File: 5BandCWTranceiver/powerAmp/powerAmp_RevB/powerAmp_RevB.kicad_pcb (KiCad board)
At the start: 2 copper layers, 59.7 x 45.7 mm, 56 parts, among them Q1 IRF530, Q5 2N2907SOT223, Q6 MOSFET-NCHANNELBS170, T1 2N2222A-SOT223, T2 2N2222A-SOT223

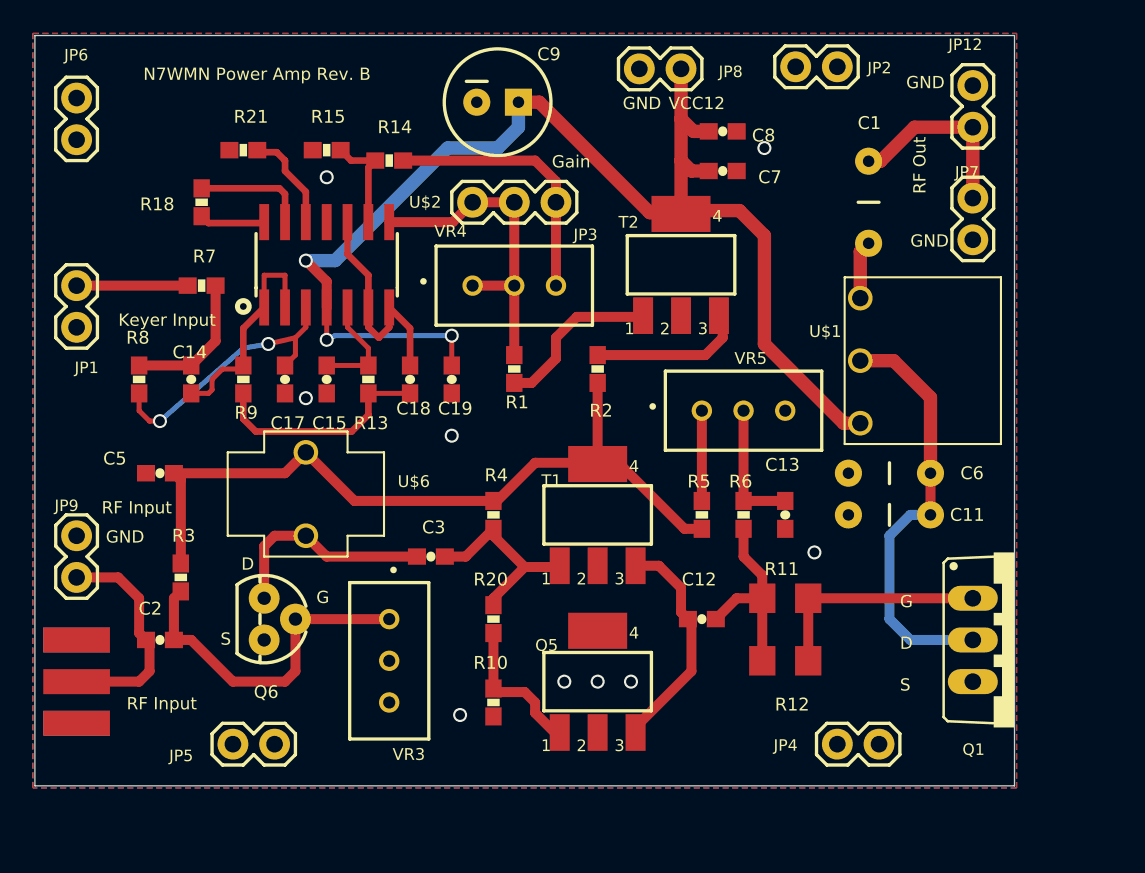
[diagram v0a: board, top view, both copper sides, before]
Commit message: Removed zip files
remove zip files
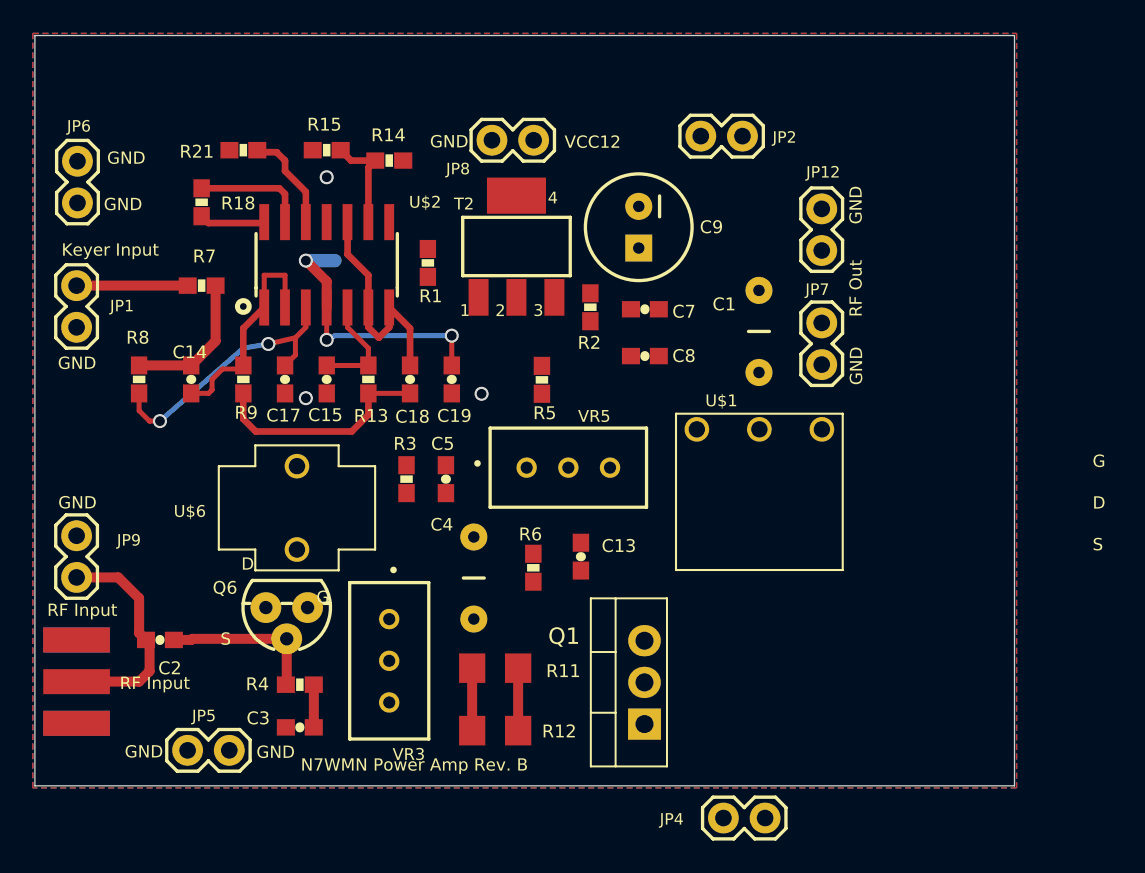
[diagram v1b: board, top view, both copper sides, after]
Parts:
- removed C11: 220p, powerAmp_RevB:CAP-PTH-5MM
- removed C12: 0.1uF, powerAmp_RevB:0603-CAP
- removed C6: 560p, powerAmp_RevB:CAP-PTH-5MM
- removed JP3: , powerAmp_RevB:1X03
- removed Q5: 2N2907SOT223, powerAmp_RevB:SOT223
- removed R10: 3.3K, powerAmp_RevB:0603-RES
- removed R20: 0, powerAmp_RevB:0603-RES
- removed T1: 2N2222A-SOT223, powerAmp_RevB:SOT223
- removed VR4: 3296W-1-505LF, powerAmp_RevB:3296W-1
- added C4: 0.1uF, powerAmp_RevB:CAP-PTH-5MM, F.Cu at (145.4, 115.2)
- C14, C18: value 0.22uF -> 710-885012206073
- C15: value 0.022uF -> 80-C0603C223K3R
- C17: value 0.1uF -> 710-885012206071
- C9: value (none) -> CAP_POLPTH1
- Q1: value IRF530 -> RD16HHF1; footprint powerAmp_RevB:TO220BV -> Package_TO_SOT_THT:TO-220-3_Vertical
- R13: value 11K -> 603-RC0603FR-0711KL
- R14: value 3K -> 603-RC0603FR-073KL
- R15: value 1K -> 603-RC0603FR-071KL
- R5: value 1.5K -> 2.2K
- R7: value 33K -> 603-RC0603FR-0733KL
- R8: value 8.2K -> 603-RC0603FR-078K2L
- R9: value 36K -> 603-RC0603FR-0736KL
- moved Q1 23.1 mm to (155.8, 124.1), turned to 90 degrees
- moved R11 18.2 mm to (146.7, 120.7)
- moved R12 18.2 mm to (146.7, 124.5)
- moved C5 17.4 mm to (143.7, 109.2), turned to -90 degrees
- moved R4 15.7 mm to (134.8, 121.7), turned to 0 degrees
- moved R3 15.0 mm to (141.3, 109.2)
- moved C8 14.5 mm to (155.8, 101.7), turned to 0 degrees
- moved R6 13.2 mm to (149.0, 114.6)
- moved C3 13.1 mm to (134.8, 124.3), turned to 0 degrees
- moved U$1 12.8 mm to (162.8, 110.0), turned to 90 degrees
- moved R5 12.8 mm to (149.6, 103.1), turned to 90 degrees
- moved C13 12.7 mm to (151.9, 113.9)
- moved JP7 11.9 mm to (166.6, 99.7)
- moved JP12 11.9 mm to (166.6, 95.2)
- moved C9 11.5 mm to (155.4, 93.8), turned to -90 degrees
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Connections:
- net VCC12 renamed /VCC12
- C2 pad 1: N$10 -> Net-(C2-Pad1)
- C3 pad 1: N$16 -> GND
- C3 pad 2: N$20 -> Net-(R3-Pad1)
- C5 pad 1: N$5 -> Net-(C5-Pad1)
- Q6 pad 1: N$20 -> Net-(Q6-Pad1)
- Q6 pad 2: N$10 -> Net-(C2-Pad1)
- R1 pad 2: N$27 -> Net-(R1-Pad2)
- R11 pad 2: N$19 -> Net-(R11-Pad2)
- R12 pad 2: N$19 -> Net-(R11-Pad2)
- R14 pad 1: N$32 -> Net-(R1-Pad2)
- R2 pad 2: N$5 -> Net-(C5-Pad1)
- R3 pad 1: N$10 -> Net-(R3-Pad1)
- R3 pad 2: N$5 -> Net-(C5-Pad1)
- R4 pad 1: N$16 -> Net-(C2-Pad1)
- R4 pad 2: N$5 -> Net-(R3-Pad1)
- R5 pad 2: N$5 -> Net-(C5-Pad1)
- U$1 pad 2: N$9 -> Net-(U$1-Pad2)
- U$2 pad 8: N$27 -> Net-(R1-Pad2)
- U$6 pad P$1: N$5 -> Net-(C5-Pad1)
- U$6 pad P$2: N$20 -> Net-(Q6-Pad1)
- VR3 pad 1: N$10 -> Net-(R3-Pad1)
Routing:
- net /VCC12: track 79.0 -> 16.6 mm
- net N$5: track 47.3 -> 0.00 mm
- net N$9: track 26.1 -> 0.00 mm
- net N$10: track 20.7 -> 0.00 mm
- net N$27: track 20.0 -> 0.00 mm
- net N$32: track 16.2 -> 0.00 mm
- net N$19: track 13.8 -> 0.00 mm
- net N$11: track 13.8 -> 0.00 mm
- net N$20: track 13.3 -> 0.00 mm
- net N$16: track 12.1 -> 0.00 mm
- net Net-(C1-Pad2): track 11.5 -> 0.00 mm
- net Net-(R1-Pad1): track 10.3 -> 0.00 mm
- net Net-(C2-Pad1): track 0.00 -> 9.72 mm
- net Net-(R2-Pad1): track 9.50 -> 0.00 mm
- net N$12: track 8.90 -> 0.00 mm
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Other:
- board text removed: "Gain"

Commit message: Initial completion of schematic and routing
Routing complete; first pass
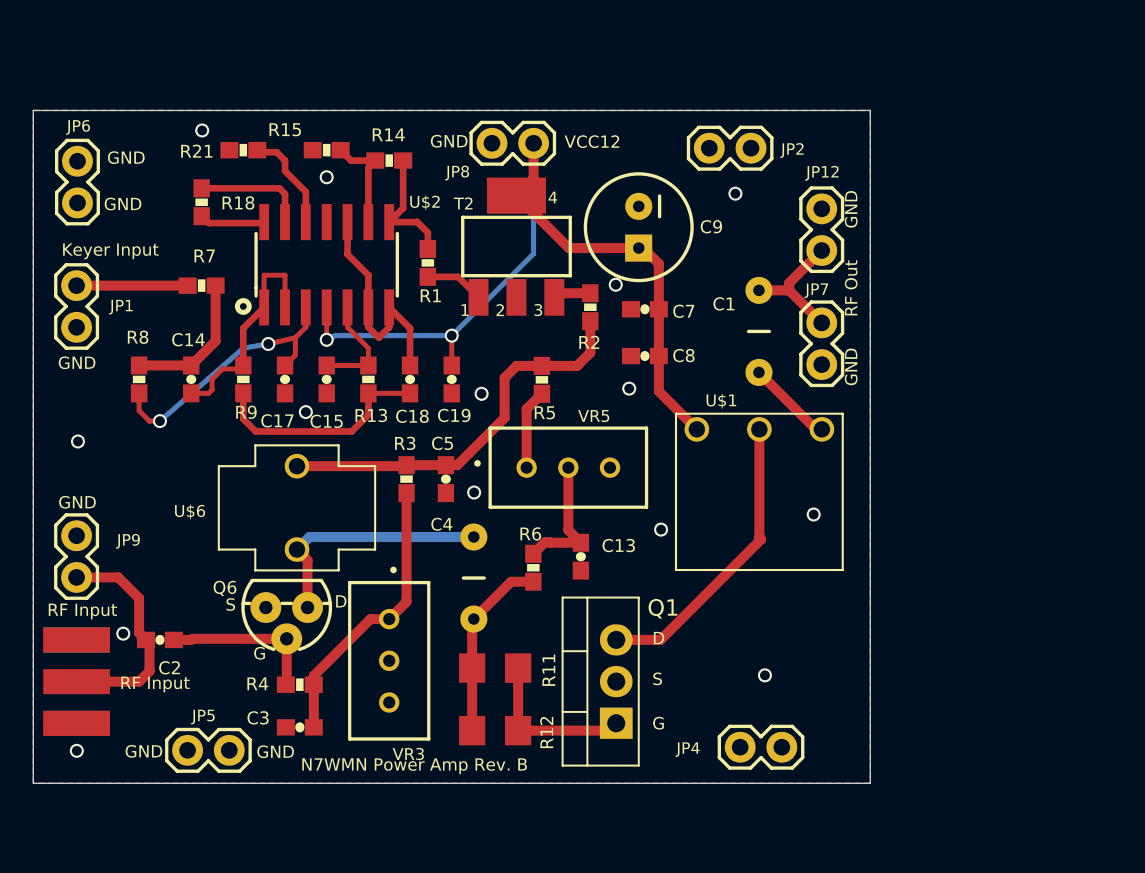
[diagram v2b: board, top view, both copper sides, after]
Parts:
- moved JP4 4.43 mm to (161.6, 125.5)
- moved Q1 1.72 mm to (154.1, 124.0)
- moved JP2 0.90 mm to (159.8, 89.0)
- moved JP8 0.18 mm to (149.0, 88.7)
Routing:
- net /VCC12: track 16.6 -> 50.7 mm, vias 3 -> 2
- net Net-(C5-Pad1): track 0.00 -> 24.1 mm
- net Net-(U$1-Pad2): track 0.00 -> 18.1 mm
- net Net-(Q6-Pad1): track 0.00 -> 14.9 mm
- net Net-(R3-Pad1): track 2.60 -> 17.3 mm
- net Net-(C13-Pad2): track 0.00 -> 8.09 mm
- net Net-(C1-Pad2): track 0.00 -> 7.90 mm
- net Net-(R1-Pad2): track 0.00 -> 7.72 mm
- net Net-(R11-Pad1): track 3.81 -> 11.4 mm
- net Net-(R11-Pad2): track 3.81 -> 9.98 mm
- net Net-(C1-Pad1): track 0.00 -> 5.27 mm
- net Net-(R5-Pad1): track 0.00 -> 4.89 mm
- net Net-(R1-Pad1): track 0.00 -> 3.61 mm
- net Net-(R2-Pad1): track 0.00 -> 2.29 mm
- net GND: vias 3 -> 14
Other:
- board size 59.7 x 45.7 mm -> 51 x 41 mm
